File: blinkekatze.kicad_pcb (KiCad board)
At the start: 2 copper layers, 69 x 69 mm, 67 parts, among them U1 ESP32-C3-MINI-1, U2 BQ40z50-R2, U3 SY8120IABC, U4 SY8120IABC, U5 SPL06-001

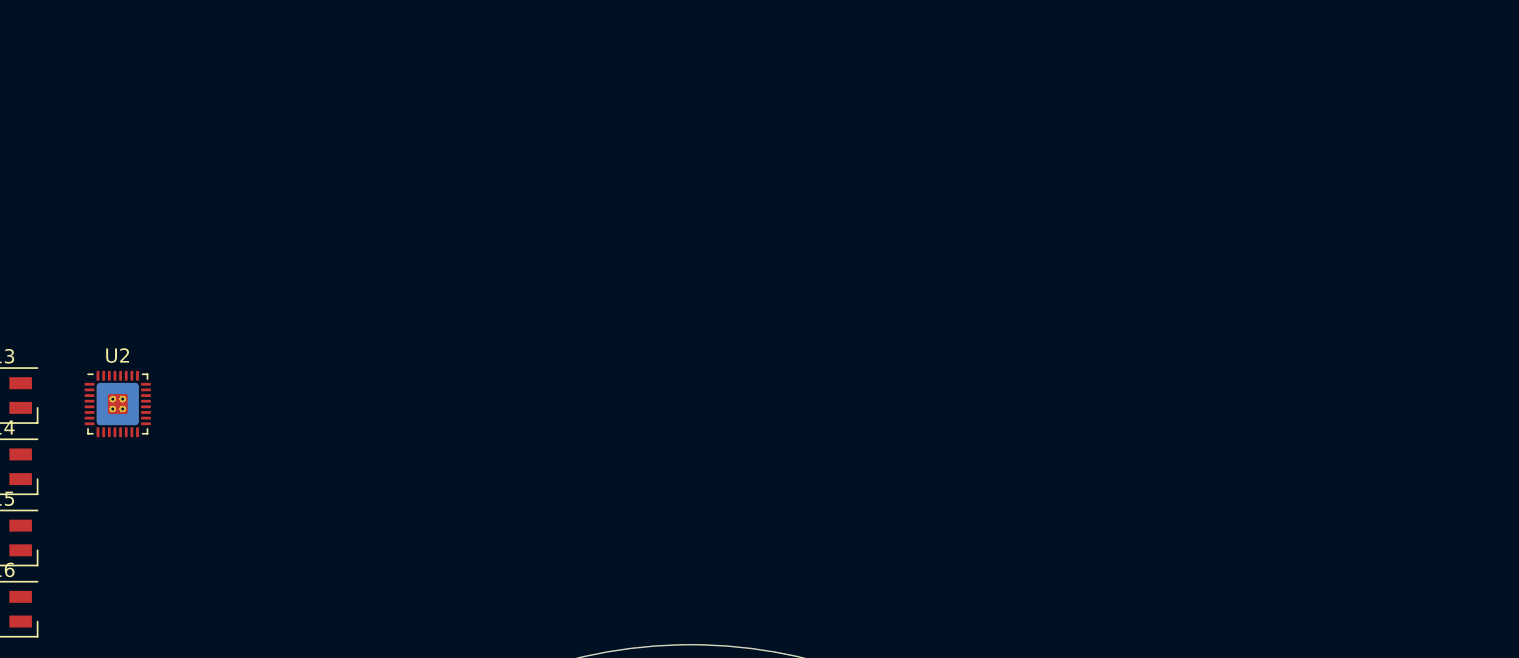
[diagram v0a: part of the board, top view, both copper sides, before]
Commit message: Finish preliminary charger and logic schematic
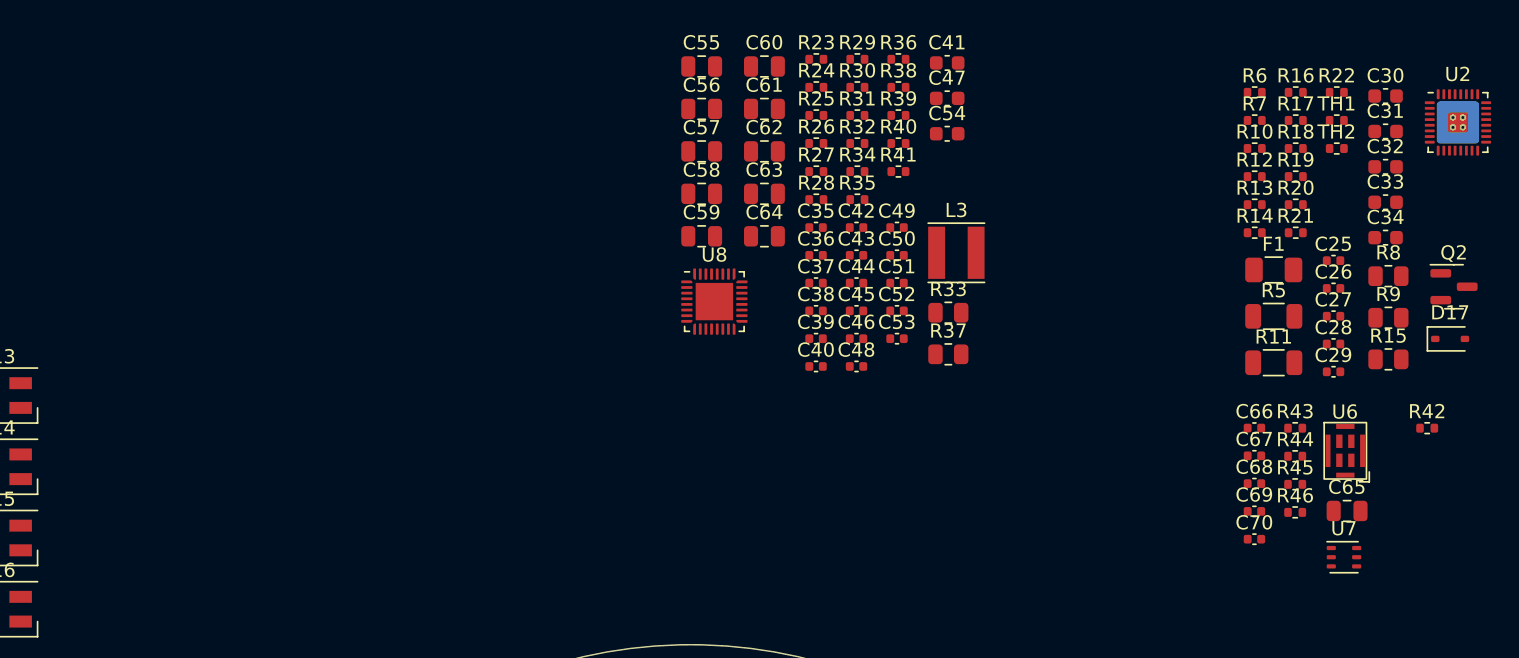
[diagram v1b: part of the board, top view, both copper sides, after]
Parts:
- added C25: 100nF, Capacitor_SMD:C_0402_1005Metric, F.Cu at (145.6, 38.3)
- added C26: 100nF, Capacitor_SMD:C_0402_1005Metric, F.Cu at (145.6, 40.2)
- added C27: 100nF, Capacitor_SMD:C_0402_1005Metric, F.Cu at (145.6, 42.2)
- added C28: 100nF, Capacitor_SMD:C_0402_1005Metric, F.Cu at (145.6, 44.2)
- added C29: 100nF, Capacitor_SMD:C_0402_1005Metric, F.Cu at (145.6, 46.1)
- added C30: 2.2uF, Capacitor_SMD:C_0603_1608Metric, F.Cu at (149.3, 26.6)
- added C31: 100nF HV, Capacitor_SMD:C_0603_1608Metric, F.Cu at (149.3, 29.1)
- added C32: 100nF HV, Capacitor_SMD:C_0603_1608Metric, F.Cu at (149.3, 31.6)
- added C33: 100nF HV, Capacitor_SMD:C_0603_1608Metric, F.Cu at (149.3, 34.1)
- added C34: 100nF HV, Capacitor_SMD:C_0603_1608Metric, F.Cu at (149.3, 36.6)
- added C35: 100nF, Capacitor_SMD:C_0402_1005Metric, F.Cu at (108.9, 35.9)
- added C36: 100nF, Capacitor_SMD:C_0402_1005Metric, F.Cu at (108.9, 37.9)
- added C37: 150pF, Capacitor_SMD:C_0402_1005Metric, F.Cu at (108.9, 39.9)
- added C38: 150pF, Capacitor_SMD:C_0402_1005Metric, F.Cu at (108.9, 41.8)
- added C39: 10nF, Capacitor_SMD:C_0402_1005Metric, F.Cu at (108.9, 43.8)
- added C40: 1uF, Capacitor_SMD:C_0402_1005Metric, F.Cu at (108.9, 45.8)
- added C41: 2.2uF, Capacitor_SMD:C_0603_1608Metric, F.Cu at (118.2, 24.2)
- added C42: 1uF, Capacitor_SMD:C_0402_1005Metric, F.Cu at (111.8, 35.9)
- added C43: 150pF, Capacitor_SMD:C_0402_1005Metric, F.Cu at (111.8, 37.9)
- added C44: 2.2nF, Capacitor_SMD:C_0402_1005Metric, F.Cu at (111.8, 39.9)
- added C45: 33pF, Capacitor_SMD:C_0402_1005Metric, F.Cu at (111.8, 41.8)
- added C46: 15pF, Capacitor_SMD:C_0402_1005Metric, F.Cu at (111.8, 43.8)
- added C47: 680pF, Capacitor_SMD:C_0603_1608Metric, F.Cu at (118.2, 26.8)
- added C48: 10nF, Capacitor_SMD:C_0402_1005Metric, F.Cu at (111.8, 45.8)
- added C49: 10nF, Capacitor_SMD:C_0402_1005Metric, F.Cu at (114.6, 35.9)
- added C50: 10nF, Capacitor_SMD:C_0402_1005Metric, F.Cu at (114.6, 37.9)
- added C51: 10nF, Capacitor_SMD:C_0402_1005Metric, F.Cu at (114.6, 39.9)
- added C52: 10nF, Capacitor_SMD:C_0402_1005Metric, F.Cu at (114.6, 41.8)
- added C53: 10nF, Capacitor_SMD:C_0402_1005Metric, F.Cu at (114.6, 43.8)
- added C54: 1uF HV, Capacitor_SMD:C_0603_1608Metric, F.Cu at (118.2, 29.3)
- added C55: 10uF HV, Capacitor_SMD:C_0805_2012Metric, F.Cu at (100.8, 24.5)
- added C56: 10uF HV, Capacitor_SMD:C_0805_2012Metric, F.Cu at (100.8, 27.5)
- added C57: 10uF HV, Capacitor_SMD:C_0805_2012Metric, F.Cu at (100.8, 30.5)
- added C58: 10uF HV, Capacitor_SMD:C_0805_2012Metric, F.Cu at (100.8, 33.5)
- added C59: 22uF, Capacitor_SMD:C_0805_2012Metric, F.Cu at (100.8, 36.5)
- added C60: 22uF, Capacitor_SMD:C_0805_2012Metric, F.Cu at (105.2, 24.5)
- added C61: 22uF, Capacitor_SMD:C_0805_2012Metric, F.Cu at (105.2, 27.5)
- added C62: 22uF, Capacitor_SMD:C_0805_2012Metric, F.Cu at (105.2, 30.5)
- added C63: 22uF, Capacitor_SMD:C_0805_2012Metric, F.Cu at (105.2, 33.5)
- added C64: 10uF, Capacitor_SMD:C_0805_2012Metric, F.Cu at (105.2, 36.5)
- added C65: 22uF, Capacitor_SMD:C_0805_2012Metric, F.Cu at (146.5, 56.0)
- added C66: 1uF, Capacitor_SMD:C_0402_1005Metric, F.Cu at (140.0, 50.1)
- added C67: 1uF, Capacitor_SMD:C_0402_1005Metric, F.Cu at (140.0, 52.1)
- added C68: 1uF, Capacitor_SMD:C_0402_1005Metric, F.Cu at (140.0, 54.1)
- added C69: 1uF, Capacitor_SMD:C_0402_1005Metric, F.Cu at (140.0, 56.0)
- added C70: 1uF, Capacitor_SMD:C_0402_1005Metric, F.Cu at (140.0, 58.0)
- added D17: 1N4148WS, Diode_SMD:D_SOD-323, F.Cu at (153.8, 43.8)
- added F1: 10A, Fuse:Fuse_1206_3216Metric, F.Cu at (141.3, 38.9)
- added L3: 2.2uH, Inductor_SMD:L_Taiyo-Yuden_MD-4040, F.Cu at (118.8, 37.7)
- added Q2: AO3401A, Package_TO_SOT_SMD:SOT-23, F.Cu at (154.1, 40.1)
- added R10: 10MR, Resistor_SMD:R_0402_1005Metric, F.Cu at (140.0, 30.3)
- added R11: 300R, Resistor_SMD:R_1206_3216Metric, F.Cu at (141.3, 45.5)
- added R12: 5.1k, Resistor_SMD:R_0402_1005Metric, F.Cu at (140.0, 32.3)
- added R13: 5.1k, Resistor_SMD:R_0402_1005Metric, F.Cu at (140.0, 34.3)
- added R14: 10MR, Resistor_SMD:R_0402_1005Metric, F.Cu at (140.0, 36.3)
- added R15: 100R 0805, Resistor_SMD:R_0805_2012Metric, F.Cu at (149.5, 45.3)
- added R16: 10k, Resistor_SMD:R_0402_1005Metric, F.Cu at (142.9, 26.3)
- added R17: 5.1k, Resistor_SMD:R_0402_1005Metric, F.Cu at (142.9, 28.3)
- added R18: 10k, Resistor_SMD:R_0402_1005Metric, F.Cu at (142.9, 30.3)
- added R19: 10MR, Resistor_SMD:R_0402_1005Metric, F.Cu at (142.9, 32.3)
- added R20: 10k, Resistor_SMD:R_0402_1005Metric, F.Cu at (142.9, 34.3)
- added R21: 10k, Resistor_SMD:R_0402_1005Metric, F.Cu at (142.9, 36.3)
- added R22: 100R, Resistor_SMD:R_0402_1005Metric, F.Cu at (145.8, 26.3)
- added R23: 10R, Resistor_SMD:R_0402_1005Metric, F.Cu at (108.9, 24.0)
- added R24: 150k, Resistor_SMD:R_0402_1005Metric, F.Cu at (108.9, 26.0)
- added R25: 100k, Resistor_SMD:R_0402_1005Metric, F.Cu at (108.9, 28.0)
- added R26: 100k, Resistor_SMD:R_0402_1005Metric, F.Cu at (108.9, 30.0)
- added R27: 27k, Resistor_SMD:R_0402_1005Metric, F.Cu at (108.9, 31.9)
- added R28: 33k, Resistor_SMD:R_0402_1005Metric, F.Cu at (108.9, 33.9)
- added R29: 10k, Resistor_SMD:R_0402_1005Metric, F.Cu at (111.8, 24.0)
- added R30: 27k, Resistor_SMD:R_0402_1005Metric, F.Cu at (111.8, 26.0)
- added R31: 10k, Resistor_SMD:R_0402_1005Metric, F.Cu at (111.8, 28.0)
- added R32: 100k, Resistor_SMD:R_0402_1005Metric, F.Cu at (111.8, 30.0)
- added R33: 10mR, Resistor_SMD:R_0805_2012Metric, F.Cu at (118.3, 42.0)
- added R34: 10R, Resistor_SMD:R_0402_1005Metric, F.Cu at (111.8, 31.9)
- added R35: 10R, Resistor_SMD:R_0402_1005Metric, F.Cu at (111.8, 33.9)
- added R36: 10R, Resistor_SMD:R_0402_1005Metric, F.Cu at (114.7, 24.0)
- added R37: 10mR, Resistor_SMD:R_0805_2012Metric, F.Cu at (118.3, 44.9)
- added R38: 10R, Resistor_SMD:R_0402_1005Metric, F.Cu at (114.7, 26.0)
- added R39: 1R, Resistor_SMD:R_0402_1005Metric, F.Cu at (114.7, 28.0)
- added R40: 100k, Resistor_SMD:R_0402_1005Metric, F.Cu at (114.7, 30.0)
- added R41: 10k, Resistor_SMD:R_0402_1005Metric, F.Cu at (114.7, 31.9)
- added R42: 100k, Resistor_SMD:R_0402_1005Metric, F.Cu at (152.2, 50.1)
- added R43: 10k, Resistor_SMD:R_0402_1005Metric, F.Cu at (142.9, 50.1)
- added R44: 100k, Resistor_SMD:R_0402_1005Metric, F.Cu at (142.9, 52.1)
- added R45: 4.7k, Resistor_SMD:R_0402_1005Metric, F.Cu at (142.9, 54.1)
- added R46: 4.7k, Resistor_SMD:R_0402_1005Metric, F.Cu at (142.9, 56.1)
- added R5: 1mR, Resistor_SMD:R_1206_3216Metric, F.Cu at (141.3, 42.2)
- added R6: 100R, Resistor_SMD:R_0402_1005Metric, F.Cu at (140.0, 26.3)
- added R7: 100R, Resistor_SMD:R_0402_1005Metric, F.Cu at (140.0, 28.3)
- added R8: 100R 0805, Resistor_SMD:R_0805_2012Metric, F.Cu at (149.5, 39.4)
- added R9: 100R 0805, Resistor_SMD:R_0805_2012Metric, F.Cu at (149.5, 42.3)
- added TH1: 10k, Resistor_SMD:R_0402_1005Metric, F.Cu at (145.8, 28.3)
- added TH2: 10k, Resistor_SMD:R_0402_1005Metric, F.Cu at (145.8, 30.3)
- added U6: ~, Package_LGA_ST:ST_HCLGA-4LD_3x4mm, F.Cu at (146.4, 51.7)
- added U7: LTR-303ALS-01, OptoDevice:Lite-On_LTR-303ALS-01, F.Cu at (146.3, 59.3)
- added U8: BQ25703A, Package_DFN_QFN:QFN-32-1EP_4x4mm_P0.4mm_EP2.65x2.65mm, F.Cu at (101.7, 41.2)
- moved U2 97.1 mm to (154.4, 28.5)
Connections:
- net /Power/VIN renamed /Charger/VSYS
- C23 pad 1: /Power/VLED -> /LEDs/VCC_LED
- C24 pad 1: /Power/VLED -> /LEDs/VCC_LED
- L2 pad 2: /Power/VLED -> /LEDs/VCC_LED
- R3 pad 1: /Power/VLED -> /LEDs/VCC_LED
- U1 pad 12: unconnected-(U1-IO0-Pad12) -> Net-(U1-IO0)
- U1 pad 13: unconnected-(U1-IO1-Pad13) -> Net-(U1-IO1)
- U1 pad 18: unconnected-(U1-IO4-Pad18) -> /Logic/LED_EN
- U1 pad 19: unconnected-(U1-IO5-Pad19) -> /LEDs/DIN
- U1 pad 20: unconnected-(U1-IO6-Pad20) -> Net-(U1-IO6)
- U1 pad 21: unconnected-(U1-IO7-Pad21) -> Net-(U1-IO7)
- U1 pad 22: unconnected-(U1-IO8-Pad22) -> Net-(U1-IO8)
- U1 pad 23: unconnected-(U1-IO9-Pad23) -> Net-(U1-IO9)
- U1 pad 26: unconnected-(U1-IO18/D--Pad26) -> /Logic/USB_D-
- U1 pad 27: unconnected-(U1-IO19/D+-Pad27) -> /Logic/USB_D+
- U1 pad 3: unconnected-(U1-3V3-Pad3) -> +3V3
- U1 pad 5: unconnected-(U1-IO2-Pad5) -> /Battery/SMBC
- U1 pad 6: unconnected-(U1-IO3-Pad6) -> /Battery/SMBD
- U1 pad 8: unconnected-(U1-EN-Pad8) -> Net-(U1-EN)
- U2 pad 1: unconnected-(U2-PBI-Pad1) -> Net-(U2-PBI)
- U2 pad 10: unconnected-(U2-TS1-Pad10) -> Net-(U2-TS1)
- U2 pad 11: unconnected-(U2-TS2-Pad11) -> Net-(U2-TS2)
- U2 pad 12: unconnected-(U2-TS3-Pad12) -> GND1
- U2 pad 13: unconnected-(U2-TS4-Pad13) -> GND1
- U2 pad 16: unconnected-(U2-~{PRES/SHDWN}-Pad16) -> Net-(U2-~{PRES/SHDWN})
- U2 pad 18: unconnected-(U2-SMBD-Pad18) -> /Battery/SMBD
- U2 pad 19: unconnected-(U2-SMBC-Pad19) -> /Battery/SMBC
- U2 pad 2: unconnected-(U2-VC4-Pad2) -> Net-(U2-VC2)
- U2 pad 23: unconnected-(U2-PTC-Pad23) -> Net-(U2-PTC)
- U2 pad 24: unconnected-(U2-PTCEN-Pad24) -> Net-(U2-PTCEN)
- U2 pad 25: unconnected-(U2-FUSE-Pad25) -> Net-(U2-FUSE)
- U2 pad 26: unconnected-(U2-VCC-Pad26) -> Net-(U2-VCC)
- U2 pad 27: unconnected-(U2-PACK-Pad27) -> Net-(U2-PACK)
- U2 pad 28: unconnected-(U2-DSG-Pad28) -> Net-(U2-DSG)
- U2 pad 3: unconnected-(U2-VC3-Pad3) -> Net-(U2-VC2)
- U2 pad 30: unconnected-(U2-PCHG-Pad30) -> Net-(U2-PCHG)
- U2 pad 31: unconnected-(U2-CHG-Pad31) -> Net-(U2-CHG)
- U2 pad 32: unconnected-(U2-BAT-Pad32) -> /Battery/BAT
- U2 pad 33: PWRPD -> GND1
- U2 pad 4: unconnected-(U2-VC2-Pad4) -> Net-(U2-VC2)
- U2 pad 5: unconnected-(U2-VC1-Pad5) -> Net-(U2-VC1)
- U2 pad 6: unconnected-(U2-SRN-Pad6) -> /Battery/PS-
- U2 pad 8: unconnected-(U2-SRP-Pad8) -> /Battery/PS+
- U2 pad 9: PWRPD -> GND1
- U4 pad 4: /Power/LED_EN -> /Logic/LED_EN
- U5 pad 2: unconnected-(U5-CSB-Pad2) -> Net-(U1-IO9)
- U5 pad 3: unconnected-(U5-SDA-Pad3) -> Net-(U1-IO7)
- U5 pad 4: unconnected-(U5-SCK-Pad4) -> Net-(U1-IO8)
- U5 pad 5: (no net) -> Net-(U1-IO6)
- U5 pad 6: unconnected-(U5-VDDIO-Pad6) -> +3V3
- U5 pad 8: unconnected-(U5-VDD-Pad8) -> +3V3

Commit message: Aesthetic top level schematic fixes
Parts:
- added Q1: AON7544, Package_DFN_FET:DFN-8-FET_3x3mm_P0.65mm, F.Cu at (93.3, 23.2)
- added Q3: AON7544, Package_DFN_FET:DFN-8-FET_3x3mm_P0.65mm, F.Cu at (93.3, 27.8)
- added Q4: CSD17308Q3, Package_DFN_FET:DFN-8-FET_3x3mm_P0.65mm, F.Cu at (86.0, 23.2)
- added Q5: CSD17308Q3, Package_DFN_FET:DFN-8-FET_3x3mm_P0.65mm, F.Cu at (86.0, 27.8)
- added Q6: CSD17308Q3, Package_DFN_FET:DFN-8-FET_3x3mm_P0.65mm, F.Cu at (86.0, 32.3)
- added Q7: CSD17308Q3, Package_DFN_FET:DFN-8-FET_3x3mm_P0.65mm, F.Cu at (86.0, 36.9)
- added Q8: CSD17308Q3, Package_DFN_FET:DFN-8-FET_3x3mm_P0.65mm, F.Cu at (86.0, 41.4)

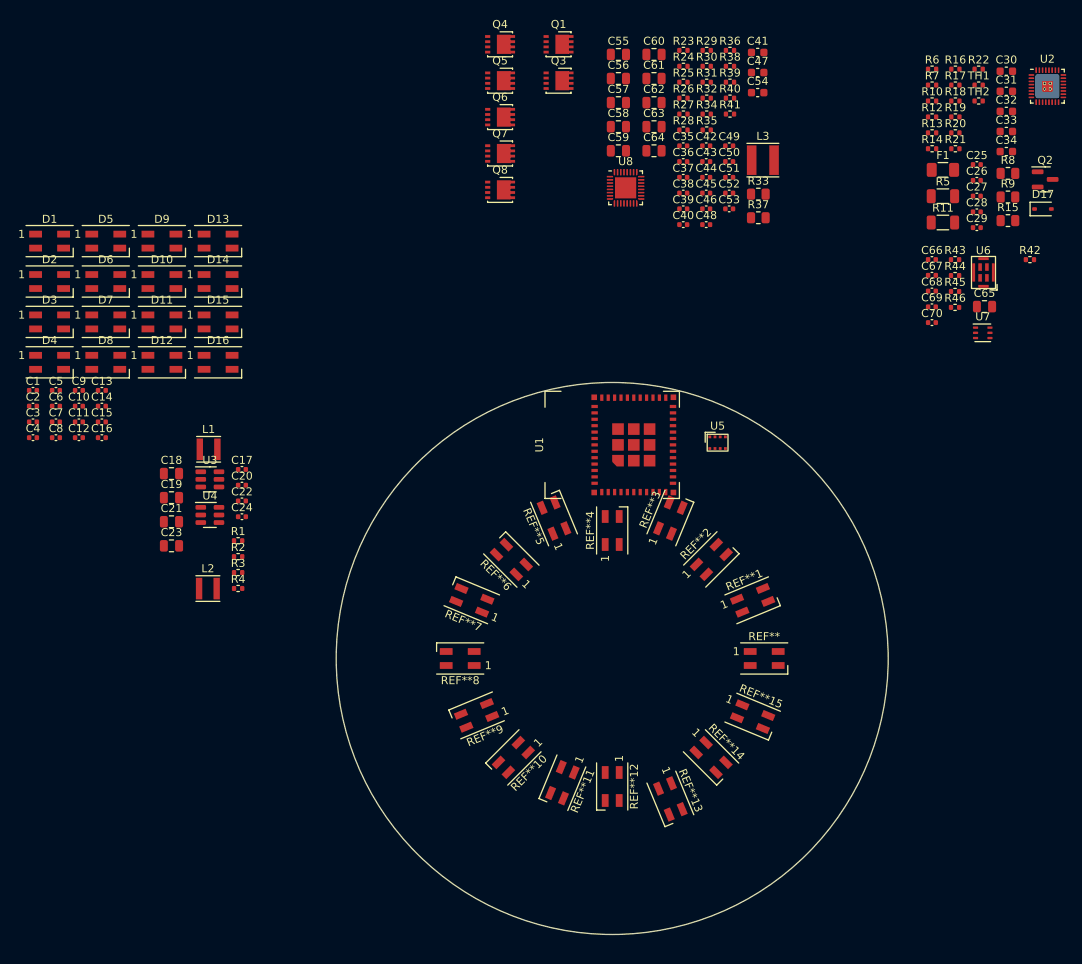
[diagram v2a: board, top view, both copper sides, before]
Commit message: Finish rough layout
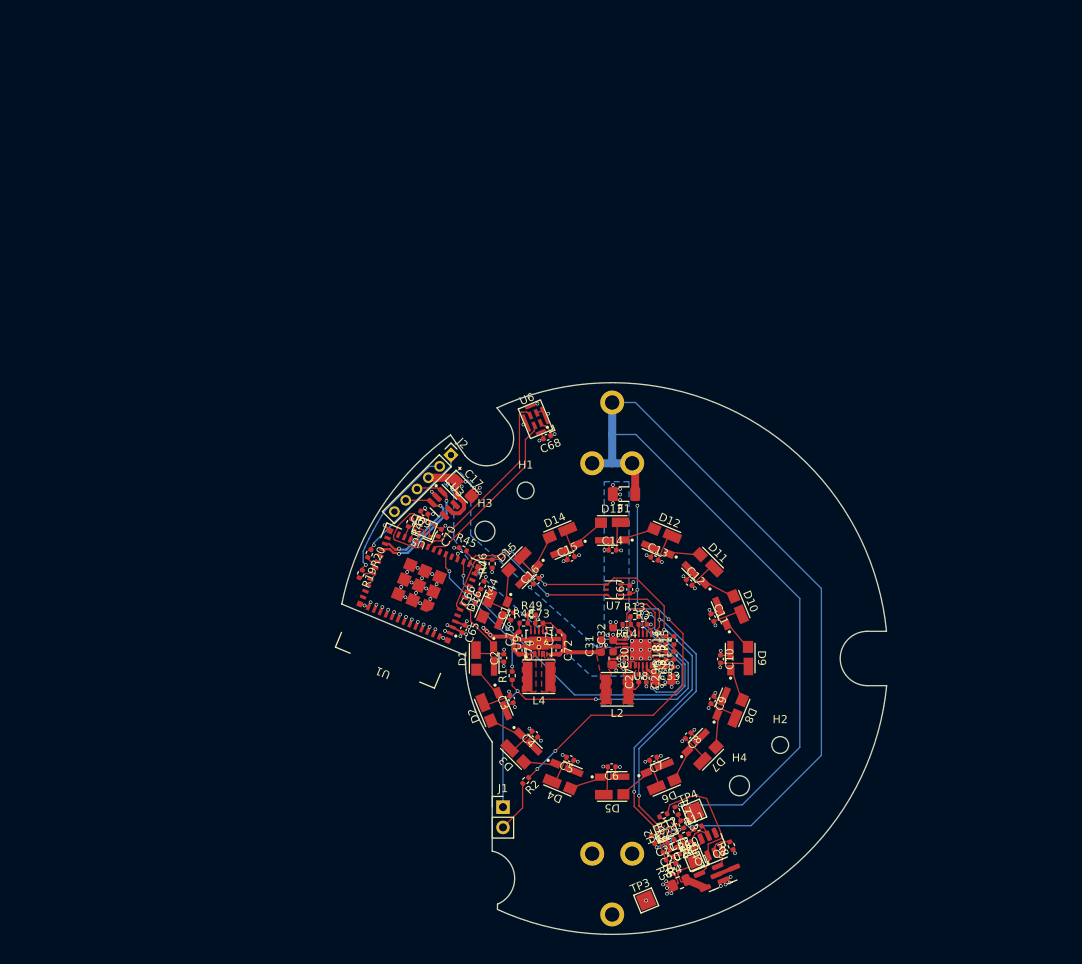
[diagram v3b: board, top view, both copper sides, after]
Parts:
- removed C18, C19, C59, C60, C61, C62, C63: 22uF, Capacitor_SMD:C_0805_2012Metric
- removed C34: 100nF HV, Capacitor_SMD:C_0603_1608Metric
- removed C35, C36: 100nF, Capacitor_SMD:C_0402_1005Metric
- removed C37, C38, C43: 150pF, Capacitor_SMD:C_0402_1005Metric
- removed C39, C48, C49, C50, C51, C52, C53: 10nF, Capacitor_SMD:C_0402_1005Metric
- removed C40, C42: 1uF, Capacitor_SMD:C_0402_1005Metric
- removed C41: 2.2uF, Capacitor_SMD:C_0603_1608Metric
- removed C44: 2.2nF, Capacitor_SMD:C_0402_1005Metric
- removed C45: 33pF, Capacitor_SMD:C_0402_1005Metric
- removed C46: 15pF, Capacitor_SMD:C_0402_1005Metric
- removed C47: 680pF, Capacitor_SMD:C_0603_1608Metric
- removed C54: 1uF HV, Capacitor_SMD:C_0603_1608Metric
- removed C55, C56, C57, C58: 10uF HV, Capacitor_SMD:C_0805_2012Metric
- removed C64: 10uF, Capacitor_SMD:C_0805_2012Metric
- removed D17: 1N4148WS, Diode_SMD:D_SOD-323
- removed L1: 4.7uH, Inductor_SMD:L_Taiyo-Yuden_MD-3030
- removed L3: 2.2uH, Inductor_SMD:L_Taiyo-Yuden_MD-4040
- removed Q3: AON7544, Package_DFN_FET:DFN-8-FET_3x3mm_P0.65mm
- removed Q4, Q5, Q6, Q7, Q8: CSD17308Q3, Package_DFN_FET:DFN-8-FET_3x3mm_P0.65mm
- removed R21, R29, R31, R41, TH1, TH2: 10k, Resistor_SMD:R_0402_1005Metric
- removed R22: 100R, Resistor_SMD:R_0402_1005Metric
- removed R23, R34, R35, R36, R38: 10R, Resistor_SMD:R_0402_1005Metric
- removed R24: 150k, Resistor_SMD:R_0402_1005Metric
- removed R25, R26, R32, R40, R42: 100k, Resistor_SMD:R_0402_1005Metric
- removed R27, R30: 27k, Resistor_SMD:R_0402_1005Metric
- removed R28: 33k, Resistor_SMD:R_0402_1005Metric
- removed R33, R37: 10mR, Resistor_SMD:R_0805_2012Metric
- removed R39: 1R, Resistor_SMD:R_0402_1005Metric
- removed REF**, REF**1, REF**10, REF**11, REF**12, REF**13, REF**14, REF**15, REF**2, REF**3, REF**4, REF**5, REF**6, REF**7, REF**8, REF**9: LED_SK6812MINI_PLCC4_3.5x3.5mm_P1.75mm, LED_SMD:LED_SK6812MINI_PLCC4_3.5x3.5mm_P1.75mm
- added BTT1: B+, Battery_Holder_MYOUNG:MY-18650-01, B.Cu at (100.0, 75.6)
- added BTT2: B-, Battery_Holder_MYOUNG:MY-18650-01, B.Cu at (100.0, 124.4)
- added C71: 10uF, Capacitor_SMD:C_0402_1005Metric, F.Cu at (93.3, 97.1)
- added C72: 10uF, Capacitor_SMD:C_0402_1005Metric, F.Cu at (93.3, 99.0)
- added C73: 100nF, Capacitor_SMD:C_0402_1005Metric, F.Cu at (90.9, 95.6)
- added C74: 10uF, Capacitor_SMD:C_0402_1005Metric, F.Cu at (88.4, 99.0)
- added C75: 10uF, Capacitor_SMD:C_0402_1005Metric, F.Cu at (88.4, 97.1)
- added H1: Left peg, MountingHole:MountingHole_2.1mm, F.Cu at (89.2, 79.0)
- added H2: Right peg, MountingHole:MountingHole_2.1mm, F.Cu at (121.0, 110.8)
- added H3: Left screw, MountingHole:MountingHole_2.5mm, F.Cu at (84.1, 84.1)
- added H4: Right screw, MountingHole:MountingHole_2.5mm, F.Cu at (115.9, 115.9)
- added J1: Power key, Connector_PinHeader_2.54mm:PinHeader_1x02_P2.54mm_Vertical, F.Cu at (86.3, 118.6)
- added J2: Conn_01x06, Connector_PinHeader_2.00mm:PinHeader_1x06_P2.00mm_Vertical, F.Cu at (79.8, 74.6)
- added L4: 2.2uH, Inductor_SMD:L_Taiyo-Yuden_MD-4040, F.Cu at (90.8, 102.3)
- added R48: 0R, Resistor_SMD:R_0402_1005Metric, F.Cu at (88.9, 95.6)
- added R49: DNP, Resistor_SMD:R_0402_1005Metric, F.Cu at (89.9, 94.6)
- added TP3: ICAL+, TestPoint:TestPoint_Pad_2.0x2.0mm, F.Cu at (104.2, 130.2)
- added TP4: VCAL, TestPoint:TestPoint_Pad_2.0x2.0mm, F.Cu at (110.2, 119.2)
- added TP5: ICAL-, TestPoint:TestPoint_Pad_1.5x1.5mm, F.Cu at (110.3, 125.4)
- added U9: TPS63001, Package_Texas:Texas_DRC0010J_ThermalVias.3, F.Cu at (90.8, 98.1)
- C17: value 100nF -> 10uF; footprint Capacitor_SMD:C_0402_1005Metric -> Capacitor_Tantalum_SMD:CP_EIA-3216-18_Kemet-A
- C20, C24: value 22pF -> 100nF
- C21, C23: value 22uF -> 100nF; footprint Capacitor_SMD:C_0805_2012Metric -> Capacitor_SMD:C_0402_1005Metric
- C25: value 100nF -> 1uF
- C28: value 100nF -> 22uF; footprint Capacitor_SMD:C_0402_1005Metric -> Capacitor_SMD:C_0805_2012Metric
- C29: value 100nF -> 4.7uF
- C30: value 2.2uF -> 10uF
- C31, C32: value 100nF HV -> 10uF
- C33: value 100nF HV -> 1uF; footprint Capacitor_SMD:C_0603_1608Metric -> Capacitor_SMD:C_0402_1005Metric
- C65: value 22uF -> 10uF; footprint Capacitor_SMD:C_0805_2012Metric -> Capacitor_SMD:C_0402_1005Metric
- D1, D10, D11, D12, D13, D14, D15, D16, D2, D3, D4, D5, D6, D7, D8, D9: value WS2812B -> SK6812MINI-012; footprint LED_SMD:LED_SK6812MINI_PLCC4_3.5x3.5mm_P1.75mm -> LED_SMD_RGB:XXXX12-X1
- F1: value 10A -> 4A
- L2: value 4.7uH -> 2.2uH; footprint Inductor_SMD:L_Taiyo-Yuden_MD-3030 -> Inductor_SMD:L_Taiyo-Yuden_MD-4040
- Q1: value AON7544 -> AO3400A; footprint Package_DFN_FET:DFN-8-FET_3x3mm_P0.65mm -> Package_TO_SOT_SMD:SOT-23
- Q2: value AO3401A -> AO3400A
- R1: value 100k -> 10k
- R10: value 10MR -> 100R
- R11: value 300R -> 470R; footprint Resistor_SMD:R_1206_3216Metric -> Resistor_SMD:R_0402_1005Metric
- R12: value 5.1k -> 100R
- R13, R17: value 5.1k -> 10k
- R14: value 10MR -> 10k
- R15, R9: value 100R 0805 -> 10k; footprint Resistor_SMD:R_0805_2012Metric -> Resistor_SMD:R_0402_1005Metric
- R19: value 10MR -> 330
- R2: value 22k -> 100R
- R20: value 10k -> 330
- R3: value 100k -> 150R
- R4: value 15k -> 10mR; footprint Resistor_SMD:R_0402_1005Metric -> Resistor_SMD:R_0805_2012Metric
- R5: value 1mR -> 100R; footprint Resistor_SMD:R_1206_3216Metric -> Resistor_SMD:R_0402_1005Metric
- R8: value 100R 0805 -> 1k; footprint Resistor_SMD:R_0805_2012Metric -> Resistor_SMD:R_0402_1005Metric
- U2: value BQ40z50-R2 -> BQ27546; footprint Package_Texas:VQFN-32-4.1x4.1-EP-1.4 -> Package_DSBGA:DSBGA-15_BQ27546_I2C_1.95x2.6mm_P0.5mm
- U3: value SY8120IABC -> SRV05-4
- U4: value SY8120IABC -> FM2113
- U8: value BQ25703A -> BQ24295; footprint Package_DFN_QFN:QFN-32-1EP_4x4mm_P0.4mm_EP2.65x2.65mm -> Package_DFN_QFN:QFN-24-1EP_4x4mm_P0.5mm_EP2.7x2.7mm
- moved Q1 105.9 mm to (112.1, 127.5), turned to 22.5 degrees
- moved R6 104.7 mm to (108.2, 126.1), turned to 112.5 degrees
- moved U2 104.5 mm to (106.7, 121.4), turned to 112.5 degrees
- moved R10 96.9 mm to (109.1, 122.1), turned to -157.5 degrees
- moved R7 96.2 mm to (108.0, 119.0), turned to -67.5 degrees
- moved Q2 95.1 mm to (114.4, 126.5), turned to 22.5 degrees
- moved R19 93.8 mm to (68.6, 89.4), turned to -112.5 degrees
- moved R12 93.5 mm to (106.4, 119.6), turned to -157.5 degrees
- moved D5 93.0 mm to (100.0, 116.0), turned to 180 degrees
- moved D6 93.0 mm to (106.1, 114.8), turned to -157.5 degrees
- moved C25 92.8 mm to (107.3, 122.8), turned to 22.5 degrees
- moved R9 91.8 mm to (105.1, 122.6), turned to -67.5 degrees
- moved D7 91.8 mm to (111.3, 111.3), turned to -135 degrees
- moved R8 90.9 mm to (114.9, 123.4), turned to 112.5 degrees
- moved R5 90.9 mm to (107.3, 126.5), turned to 112.5 degrees
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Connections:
- C1 pad 2: /LEDs/VCC_LED -> /Charger/VLED
- C10 pad 2: /LEDs/VCC_LED -> /Charger/VLED
- C11 pad 2: /LEDs/VCC_LED -> /Charger/VLED
- C12 pad 2: /LEDs/VCC_LED -> /Charger/VLED
- C13 pad 2: /LEDs/VCC_LED -> /Charger/VLED
- C14 pad 2: /LEDs/VCC_LED -> /Charger/VLED
- C15 pad 2: /LEDs/VCC_LED -> /Charger/VLED
- C16 pad 2: /LEDs/VCC_LED -> /Charger/VLED
- C17 pad 1: Net-(U3-BS) -> VBUS
- C17 pad 2: Net-(U3-LX) -> GND
- C2 pad 2: /LEDs/VCC_LED -> /Charger/VLED
- C20 pad 1: +3V3 -> GND1
- C20 pad 2: Net-(U3-FB) -> Net-(U2-SRP)
- C21 pad 1: /Charger/VSYS -> Net-(U2-SRP)
- C21 pad 2: GND -> Net-(U2-SRN)
- C22 pad 1: Net-(U4-BS) -> Net-(U2-SRN)
- C22 pad 2: Net-(U4-LX) -> GND1
- C23 pad 1: /LEDs/VCC_LED -> Net-(U2-BAT)
- C23 pad 2: GND -> GND1
- C24 pad 1: /LEDs/VCC_LED -> Net-(U2-REGIN)
- C24 pad 2: Net-(U4-FB) -> GND1
- C25 pad 1: /Battery/PS+ -> GND1
- C25 pad 2: /Battery/PS- -> Net-(U2-VCC)
- C26 pad 1: /Battery/PS- -> Net-(Q1-S)
- C26 pad 2: GND1 -> Net-(U4-VDD)
- C27 pad 1: Net-(U2-VC2) -> Net-(C27-Pad1)
- C27 pad 2: Net-(U2-VC1) -> Net-(U8-BTST)
- C28 pad 1: Net-(U2-VC1) -> /Charger/VLED
- C28 pad 2: GND1 -> GND
- C29 pad 1: /Battery/PS+ -> Net-(U8-REGN)
- C29 pad 2: GND1 -> GND
- C3 pad 2: /LEDs/VCC_LED -> /Charger/VLED
- C30 pad 1: GND1 -> /Charger/VSYS
- C30 pad 2: Net-(U2-PBI) -> GND
- C31 pad 1: /Battery/B+ -> /Charger/VSYS
- C31 pad 2: Net-(C31-Pad2) -> GND
- C32 pad 1: Net-(C31-Pad2) -> /VBAT
- C32 pad 2: /Battery/VBAT -> GND
- C33 pad 1: Net-(C33-Pad1) -> GND
- C33 pad 2: /Battery/VBAT -> VBUS
- C4 pad 2: /LEDs/VCC_LED -> /Charger/VLED
- C5 pad 2: /LEDs/VCC_LED -> /Charger/VLED
- C6 pad 2: /LEDs/VCC_LED -> /Charger/VLED
- C7 pad 2: /LEDs/VCC_LED -> /Charger/VLED
- C8 pad 2: /LEDs/VCC_LED -> /Charger/VLED
- C9 pad 2: /LEDs/VCC_LED -> /Charger/VLED
- D1 pad 1: /LEDs/VCC_LED -> /LEDs/DIN
- D1 pad 2: Net-(D1-DOUT) -> /Charger/VLED
- D1 pad 3: GND -> Net-(D1-DOUT)
- D1 pad 4: /LEDs/DIN -> GND
- D10 pad 1: /LEDs/VCC_LED -> Net-(D10-DIN)
- D10 pad 2: Net-(D10-DOUT) -> /Charger/VLED
- D10 pad 3: GND -> Net-(D10-DOUT)
- D10 pad 4: Net-(D10-DIN) -> GND
- D11 pad 1: /LEDs/VCC_LED -> Net-(D10-DOUT)
- D11 pad 2: Net-(D11-DOUT) -> /Charger/VLED
- D11 pad 3: GND -> Net-(D11-DOUT)
- D11 pad 4: Net-(D10-DOUT) -> GND
- D12 pad 1: /LEDs/VCC_LED -> Net-(D11-DOUT)
- D12 pad 2: Net-(D12-DOUT) -> /Charger/VLED
- D12 pad 3: GND -> Net-(D12-DOUT)
- D12 pad 4: Net-(D11-DOUT) -> GND
- D13 pad 1: /LEDs/VCC_LED -> Net-(D12-DOUT)
- D13 pad 2: Net-(D13-DOUT) -> /Charger/VLED
- D13 pad 3: GND -> Net-(D13-DOUT)
- D13 pad 4: Net-(D12-DOUT) -> GND
- D14 pad 1: /LEDs/VCC_LED -> Net-(D13-DOUT)
- D14 pad 2: Net-(D14-DOUT) -> /Charger/VLED
- D14 pad 3: GND -> Net-(D14-DOUT)
- D14 pad 4: Net-(D13-DOUT) -> GND
- D15 pad 1: /LEDs/VCC_LED -> Net-(D14-DOUT)
- D15 pad 2: Net-(D15-DOUT) -> /Charger/VLED
- D15 pad 3: GND -> Net-(D15-DOUT)
- D15 pad 4: Net-(D14-DOUT) -> GND
- D16 pad 1: /LEDs/VCC_LED -> Net-(D15-DOUT)
- D16 pad 2: unconnected-(D16-DOUT-Pad2) -> /Charger/VLED
- D16 pad 3: GND -> unconnected-(D16-DOUT-Pad3)
- D16 pad 4: Net-(D15-DOUT) -> GND
- D2 pad 1: /LEDs/VCC_LED -> Net-(D1-DOUT)
- D2 pad 2: Net-(D2-DOUT) -> /Charger/VLED
- D2 pad 3: GND -> Net-(D2-DOUT)
- D2 pad 4: Net-(D1-DOUT) -> GND
- D3 pad 1: /LEDs/VCC_LED -> Net-(D2-DOUT)
- D3 pad 2: Net-(D3-DOUT) -> /Charger/VLED
- D3 pad 3: GND -> Net-(D3-DOUT)
- D3 pad 4: Net-(D2-DOUT) -> GND
- D4 pad 1: /LEDs/VCC_LED -> Net-(D3-DOUT)
- D4 pad 2: Net-(D4-DOUT) -> /Charger/VLED
- D4 pad 3: GND -> Net-(D4-DOUT)
- D4 pad 4: Net-(D3-DOUT) -> GND
- D5 pad 1: /LEDs/VCC_LED -> Net-(D4-DOUT)
- D5 pad 2: Net-(D5-DOUT) -> /Charger/VLED
- D5 pad 3: GND -> Net-(D5-DOUT)
- D5 pad 4: Net-(D4-DOUT) -> GND
- D6 pad 1: /LEDs/VCC_LED -> Net-(D5-DOUT)
- D6 pad 2: Net-(D6-DOUT) -> /Charger/VLED
- D6 pad 3: GND -> Net-(D6-DOUT)
- D6 pad 4: Net-(D5-DOUT) -> GND
- D7 pad 1: /LEDs/VCC_LED -> Net-(D6-DOUT)
- D7 pad 2: Net-(D7-DOUT) -> /Charger/VLED
- D7 pad 3: GND -> Net-(D7-DOUT)
- D7 pad 4: Net-(D6-DOUT) -> GND
- D8 pad 1: /LEDs/VCC_LED -> Net-(D7-DOUT)
- D8 pad 2: Net-(D8-DOUT) -> /Charger/VLED
- D8 pad 3: GND -> Net-(D8-DOUT)
- D8 pad 4: Net-(D7-DOUT) -> GND
- D9 pad 1: /LEDs/VCC_LED -> Net-(D8-DOUT)
- D9 pad 2: Net-(D10-DIN) -> /Charger/VLED
- D9 pad 3: GND -> Net-(D10-DIN)
- D9 pad 4: Net-(D8-DOUT) -> GND
- F1 pad 1: /Battery/VBAT -> +BATT
- F1 pad 2: /Battery/BAT+ -> /VBAT
- L2 pad 1: Net-(U4-LX) -> Net-(C27-Pad1)
- L2 pad 2: /LEDs/VCC_LED -> /Charger/VSYS
- Q1 pad 1: /Battery/B+ -> Net-(Q1-G)
- Q1 pad 2: /Battery/B+ -> Net-(Q1-S)
- Q1 pad 3: /Battery/B+ -> Net-(Q1-D)
- Q2 pad 2: /Battery/VCOM -> GND
- Q2 pad 3: Net-(Q2-D) -> Net-(Q1-D)
- R1 pad 1: +3V3 -> /Charger/PWR_ON
- R1 pad 2: Net-(U3-FB) -> Net-(U1-IO10)
- R10 pad 1: Net-(Q1-G) -> +BATT
- R10 pad 2: /Battery/B+ -> Net-(U2-REGIN)
- R11 pad 1: /Battery/B+ -> +BATT
- R11 pad 2: Net-(Q2-D) -> Net-(U4-VDD)
- R12 pad 1: Net-(U2-CHG) -> Net-(Q1-G)
- R12 pad 2: Net-(Q1-G) -> /Battery/DSG
- R13 pad 1: Net-(U2-PCHG) -> Net-(U8-TS)
- R13 pad 2: Net-(Q2-G) -> Net-(U8-REGN)
- R14 pad 1: Net-(Q2-G) -> Net-(U8-TS)
- R14 pad 2: /Battery/VCOM -> GND
- R15 pad 1: Net-(U2-VCC) -> Net-(U8-D+)
- R15 pad 2: /Battery/VCOM -> GND
- R16 pad 1: Net-(U2-~{PRES/SHDWN}) -> Net-(U8-D-)
- R16 pad 2: GND1 -> GND
- R17 pad 1: Net-(U2-DSG) -> VBUS
- R17 pad 2: Net-(Q3-G) -> Net-(U8-D+)
- R18 pad 1: GND1 -> VBUS
- R18 pad 2: Net-(U2-FUSE) -> Net-(U8-D-)
- R19 pad 1: Net-(Q3-G) -> /Logic/LED2
- R19 pad 2: /Battery/VBAT -> Net-(U1-TXD0)
- R2 pad 1: Net-(U3-FB) -> /VBAT
- R2 pad 2: GND -> Net-(J1-Pin_2)
- R20 pad 1: Net-(U2-PTC) -> /Logic/LED1
- R20 pad 2: /Battery/BAT -> Net-(U1-RXD0)
- R3 pad 1: /LEDs/VCC_LED -> Net-(U8-ILIM)
- R3 pad 2: Net-(U4-FB) -> GND
- R4 pad 1: Net-(U4-FB) -> GND1
- R4 pad 2: GND -> Net-(Q1-S)
- R45 pad 2: /Battery/SMBD -> /Battery/SDA
- R46 pad 2: /Battery/SMBC -> /Battery/SCL
- R5 pad 2: GND -> Net-(U2-SRP)
- R6 pad 1: GND1 -> Net-(Q1-S)
- R6 pad 2: /Battery/PS+ -> Net-(U2-SRN)
- R7 pad 1: GND -> +BATT
- R7 pad 2: /Battery/PS- -> Net-(U2-BAT)
- R8 pad 1: /Battery/B+ -> GND
- R8 pad 2: Net-(U2-VC2) -> Net-(U4-VM)
- R9 pad 1: Net-(B1A--) -> Net-(U2-TS)
- R9 pad 2: Net-(U2-VC1) -> Net-(U2-VCC)
- U1 pad 12: Net-(U1-IO0) -> /Battery/SDA
- U1 pad 13: Net-(U1-IO1) -> /Charger/~{CHARGE_ENABLE}
- U1 pad 16: unconnected-(U1-IO10-Pad16) -> Net-(U1-IO10)
- U1 pad 18: /Logic/LED_EN -> Net-(U1-IO4)
- U1 pad 19: /LEDs/DIN -> Net-(U1-IO5)
- U1 pad 30: unconnected-(U1-RXD0-Pad30) -> Net-(U1-RXD0)
- U1 pad 31: unconnected-(U1-TXD0-Pad31) -> Net-(U1-TXD0)
- U1 pad 5: /Battery/SMBC -> /Battery/SCL
- U1 pad 6: /Battery/SMBD -> /LEDs/DIN
- U3 pad 1: Net-(U3-BS) -> /Logic/USB_D+
- U3 pad 3: Net-(U3-FB) -> /Logic/USB_D-
- U3 pad 4: /Charger/VSYS -> unconnected-(U3-IO3-Pad4)
- U3 pad 5: /Charger/VSYS -> VBUS
- U3 pad 6: Net-(U3-LX) -> unconnected-(U3-IO4-Pad6)
- U4 pad 1: Net-(U4-BS) -> Net-(Q1-G)
- U4 pad 2: GND -> Net-(U4-VM)
- U4 pad 3: Net-(U4-FB) -> Net-(Q2-G)
- U4 pad 4: /Logic/LED_EN -> unconnected-(U4-NC-Pad4)
- U4 pad 5: /Charger/VSYS -> Net-(U4-VDD)
- U4 pad 6: Net-(U4-LX) -> Net-(Q1-S)
- U6 pad 3: Net-(U1-IO0) -> Net-(U1-IO5)
- U6 pad 4: Net-(U1-IO1) -> Net-(U1-IO4)
- U7 pad 4: /Battery/SMBC -> /Battery/SCL
- U7 pad 6: /Battery/SMBD -> /Battery/SDA
- U8 pad 1: Net-(U8-VBUS) -> VBUS
- U8 pad 10: unconnected-(U8-PSYS-Pad10) -> Net-(U8-ILIM)
- U8 pad 11: unconnected-(U8-~{PROCHOT}-Pad11) -> Net-(U8-TS)
- U8 pad 12: /Battery/SMBD -> /Charger/PWR_ON
- U8 pad 13: /Battery/SMBC -> /VBAT
- U8 pad 14: GND -> /VBAT
- U8 pad 15: unconnected-(U8-CMPOUT-Pad15) -> /Charger/VSYS
- U8 pad 16: Net-(U8-COMP1) -> /Charger/VSYS
- U8 pad 17: Net-(U8-COMP2) -> GND
- U8 pad 18: Net-(U8-CELL_BATPRESZ) -> GND
- U8 pad 19: Net-(U8-SRN) -> Net-(C27-Pad1)
- U8 pad 2: Net-(U8-ACN) -> Net-(U8-D+)
- U8 pad 20: Net-(U8-SRP) -> Net-(C27-Pad1)
- U8 pad 21: Net-(Q8-G) -> Net-(U8-BTST)
- U8 pad 22: /Charger/VSYS -> Net-(U8-REGN)
- U8 pad 23: Net-(U8-SW2) -> /Charger/VLED
- U8 pad 24: Net-(Q6-G) -> VBUS
- U8 pad 25: Net-(U8-BTST2) -> GND
- U8 pad 3: Net-(U8-ACP) -> Net-(U8-D-)
- U8 pad 4: /Charger/CHRG_OK -> unconnected-(U8-STAT-Pad4)
- U8 pad 5: /Charger/EN_OTG -> /Battery/SCL
- U8 pad 6: Net-(U8-ILIM_HIZ) -> /Battery/SDA
- U8 pad 7: Net-(U8-VDDA) -> unconnected-(U8-INT-Pad7)
- U8 pad 8: Net-(U8-IADPT) -> +3V3
- U8 pad 9: unconnected-(U8-IBAT-Pad9) -> /Charger/~{CHARGE_ENABLE}
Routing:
- net +BATT: track 0.00 -> 164.5 mm, vias 0 -> 2
- net GND: track 0.00 -> 119.0 mm, vias 0 -> 94
- net /Charger/VLED: track 0.00 -> 75.3 mm, vias 0 -> 19
- net /Battery/SCL: track 0.00 -> 70.4 mm, vias 0 -> 4
- net /Battery/SDA: track 0.00 -> 64.9 mm, vias 0 -> 4
- net /Charger/PWR_ON: track 0.00 -> 56.8 mm, vias 0 -> 3
- net /VBAT: track 0.00 -> 50.3 mm, vias 0 -> 12
- net /Charger/~{CHARGE_ENABLE}: track 0.00 -> 49.4 mm, vias 0 -> 2
- net +3V3: track 0.00 -> 43.1 mm, vias 0 -> 15
- net Net-(U1-IO5): track 0.00 -> 23.4 mm
- net Net-(U1-IO4): track 0.00 -> 21.3 mm
- net VBUS: track 0.00 -> 21.2 mm, vias 0 -> 8
- net Net-(U8-REGN): track 0.00 -> 19.2 mm, vias 0 -> 2
- net Net-(U1-IO10): track 0.00 -> 18.1 mm, vias 0 -> 2
- net /Logic/LED2: track 0.00 -> 17.6 mm, vias 0 -> 1
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- added copper zone on In2.Cu, net +3V3
- added copper zone on In2.Cu, net /Charger/VLED
- added copper zone on F.Cu, net /Charger/VSYS
- added copper zone on B.Cu, net /VBAT
- added copper zone on F.Cu, net GND
- added copper zone on In1.Cu, net GND
- added copper zone on In1.Cu, net GND1
- added copper zone on F.Cu, net Net-(C27-Pad1)
- added copper zone on F.Cu, net Net-(U9-L1)
- added copper zone on F.Cu, net Net-(U9-L2)
- added copper zone on B.Cu, net VBUS
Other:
- board size 69 x 69 mm -> 68.1 x 69 mm
- copper layers 2 -> 4
